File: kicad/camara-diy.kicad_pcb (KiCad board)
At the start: 2 copper layers, 67 x 47 mm, 23 parts, among them J1 GC9A01_8P, J3 Batería 18650, SW1 Shutter, SW2 Modo, U1 XIAO-ESP32-S3-SMD, U2 TP4056-42-ESOP8

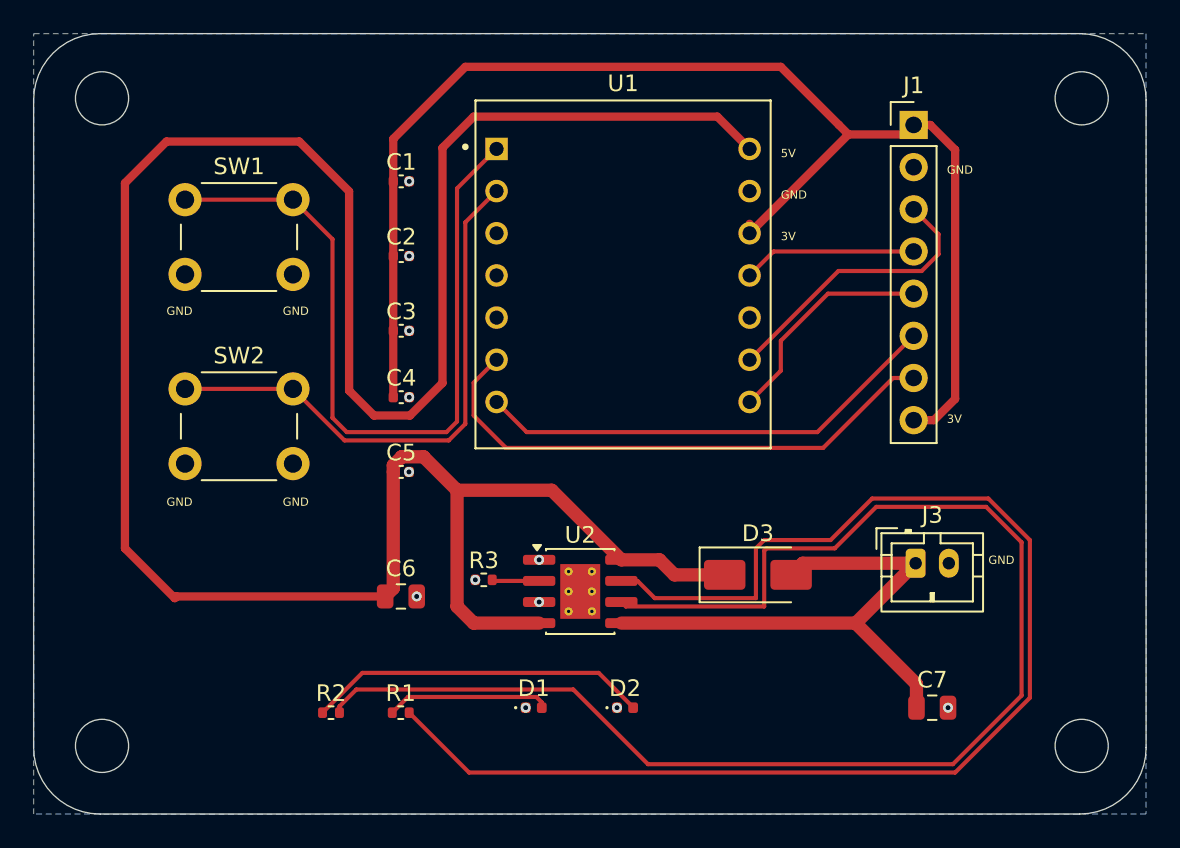
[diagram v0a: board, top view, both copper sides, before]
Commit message: pcb actualizada sin modelos 3d
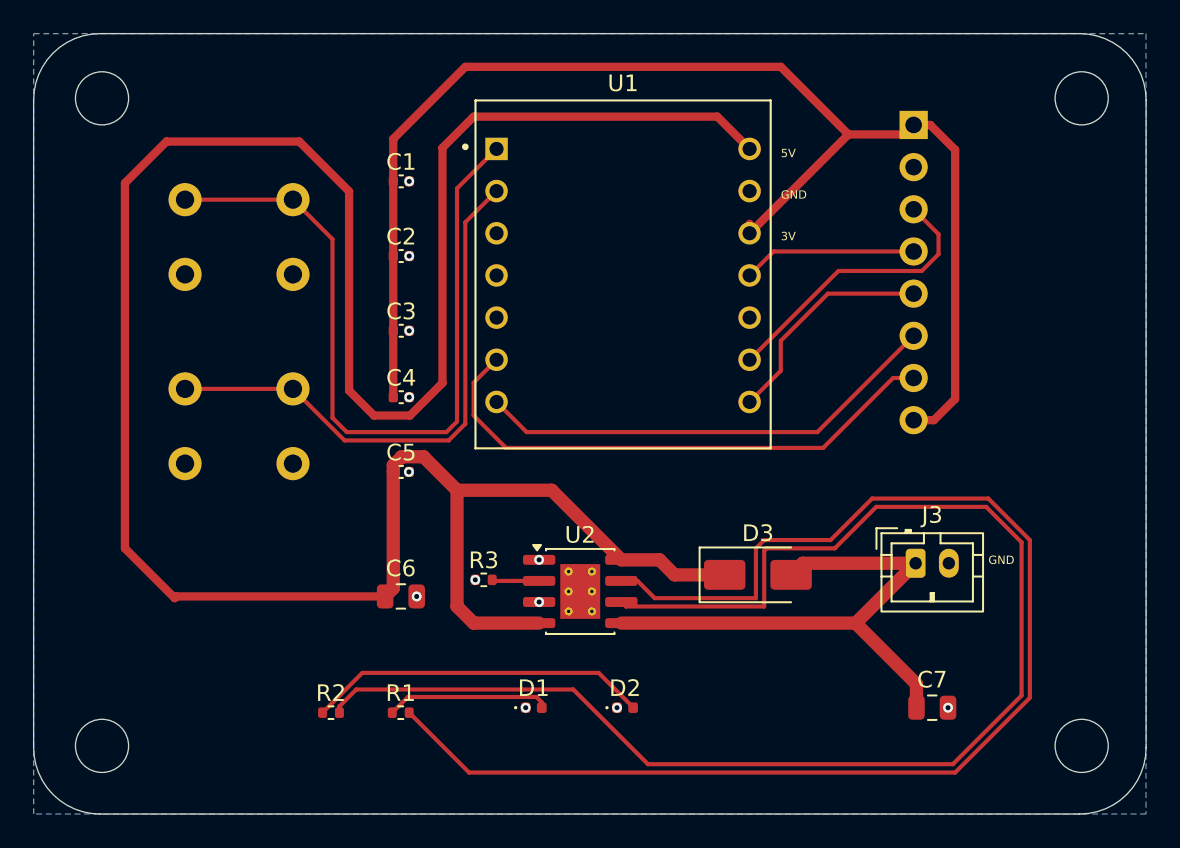
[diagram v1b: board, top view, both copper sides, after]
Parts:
- J1, SW1, SW2: moved to B.Cu
- moved SW1 6.50 mm to (123.1, 92.0), turned to 180 degrees
- moved SW2 6.50 mm to (123.1, 103.4), turned to 180 degrees
- turned J1 to 180 degrees
